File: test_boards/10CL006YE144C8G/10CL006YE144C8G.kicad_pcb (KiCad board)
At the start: 2 copper layers, 81 parts, among them IC401 10CL006YE144C8G, J401 CL_JTAG, U401 W25Q128JVS, Y401 SG-7050CAN

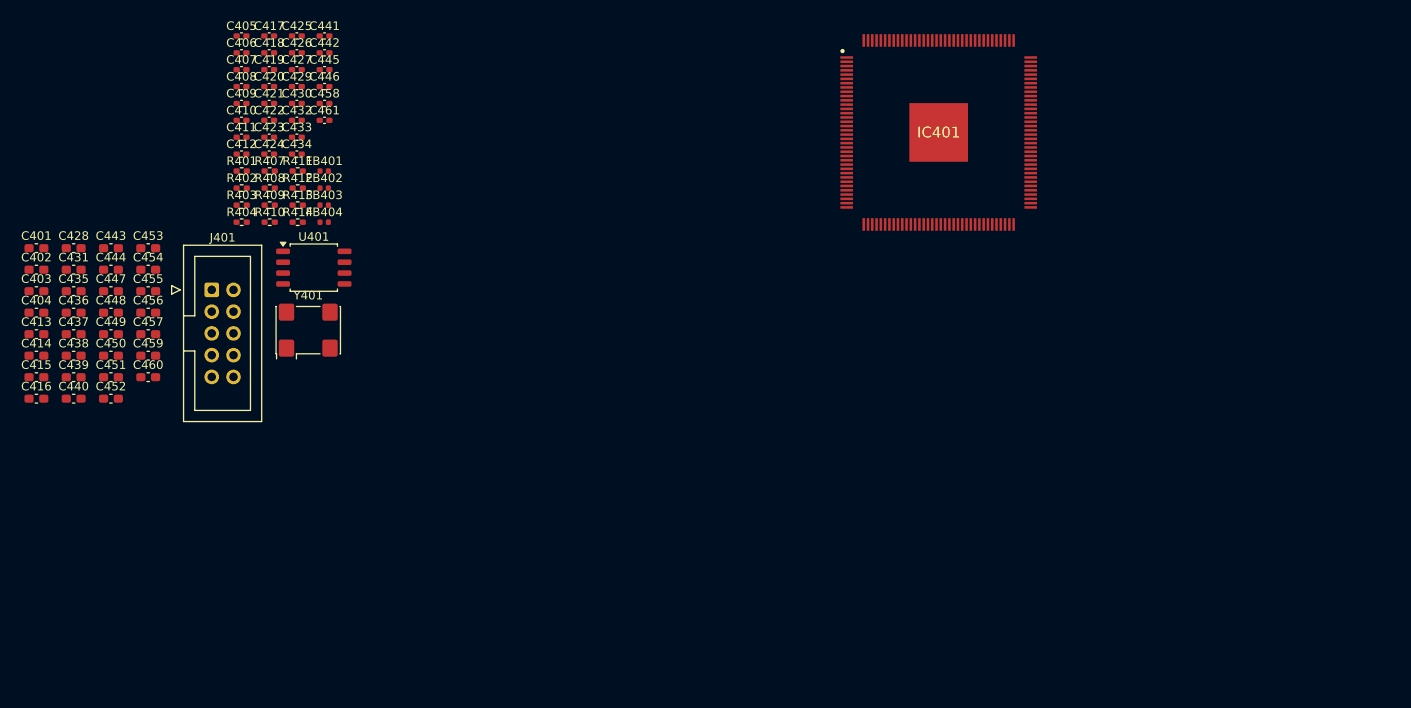
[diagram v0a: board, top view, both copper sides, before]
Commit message: Исправлена схема платы. Добавлен конфиг 10CL006.yaml
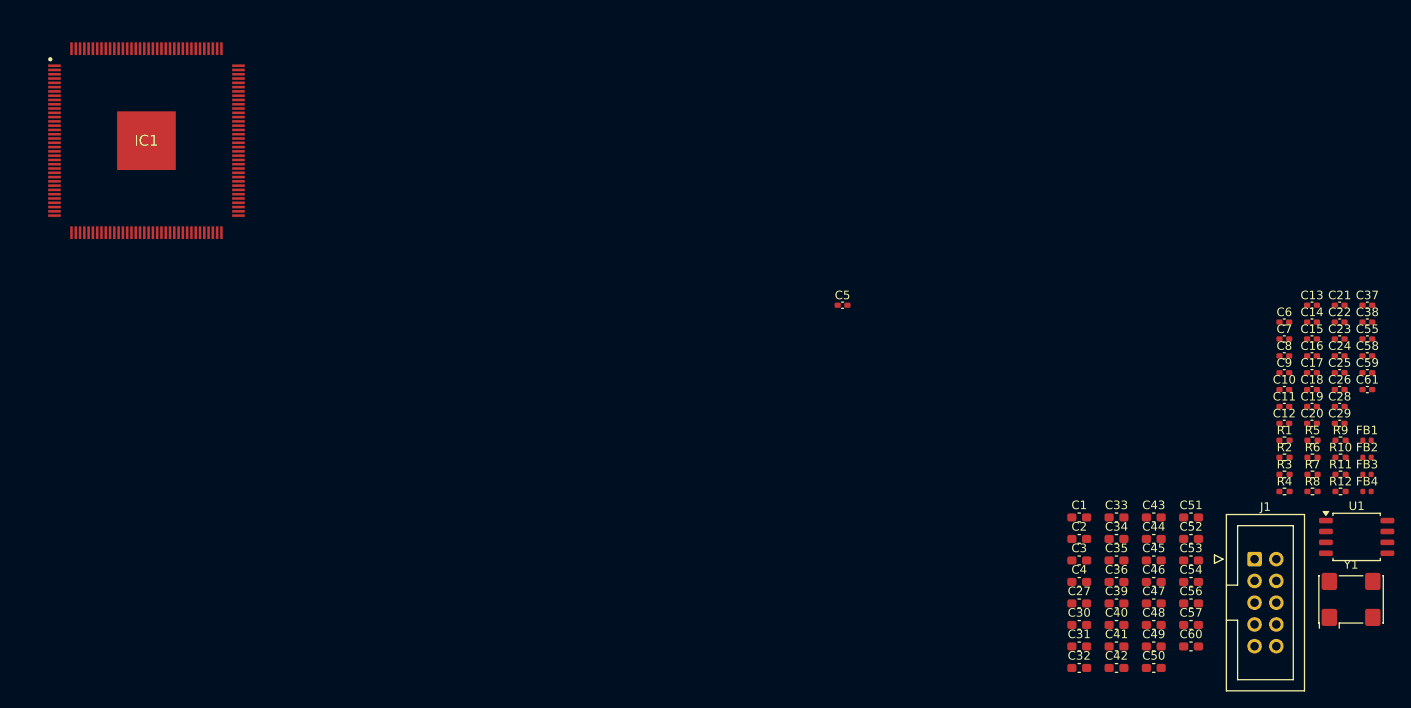
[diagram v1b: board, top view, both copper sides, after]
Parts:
- removed C401, C402, C403, C404, C435, C436, C437, C438, C439, C440, C443, C444: 1uF, Capacitor_SMD:C_0603_1608Metric_Pad1.08x0.95mm_HandSolder
- removed C405, C406, C407, C408, C409, C410, C411, C412, C417, C418, C419, C420, C421, C422, C423, C424, C425, C426, C427, C429, C430, C432, C433, C434, C441, C442, C445, C446, C458, C461: 100 nF, Capacitor_SMD:C_0402_1005Metric_Pad0.74x0.62mm_HandSolder
- removed C413, C414, C415, C416, C428, C431, C447, C448, C449, C450, C451, C452, C453, C454, C455, C456, C457, C459, C460: 4.7 uF, Capacitor_SMD:C_0603_1608Metric_Pad1.08x0.95mm_HandSolder
- removed FB401, FB402, FB403, FB404: BLM15PD121SN1D, Inductor_SMD:L_0402_1005Metric
- removed IC401: 10CL006YE144C8G, Custom_Altera_FPGA:QFP50P2200X2200X165-145N
- removed J401: CL_JTAG, Connector_IDC:IDC-Header_2x05_P2.54mm_Vertical
- removed R401: 33, Resistor_SMD:R_0402_1005Metric_Pad0.72x0.64mm_HandSolder
- removed R402, R403, R408, R409: 2R2, Resistor_SMD:R_0402_1005Metric_Pad0.72x0.64mm_HandSolder
- removed R404: 1K, Resistor_SMD:R_0402_1005Metric_Pad0.72x0.64mm_HandSolder
- removed R407, R413, R414: 4.7K, Resistor_SMD:R_0402_1005Metric_Pad0.72x0.64mm_HandSolder
- removed R410, R411, R412: 10K, Resistor_SMD:R_0402_1005Metric_Pad0.72x0.64mm_HandSolder
- removed U401: W25Q128JVS, Package_SO:SOIC-8_5.3x5.3mm_P1.27mm
- removed Y401: SG-7050CAN, Oscillator:Oscillator_SMD_SeikoEpson_SG8002CA-4Pin_7.0x5.0mm
- added C1: 1uF, Capacitor_SMD:C_0603_1608Metric_Pad1.08x0.95mm_HandSolder, F.Cu at (181.3, 115.7)
- added C10: 100 nF, Capacitor_SMD:C_0402_1005Metric_Pad0.74x0.62mm_HandSolder, F.Cu at (205.2, 100.8)
- added C11: 100 nF, Capacitor_SMD:C_0402_1005Metric_Pad0.74x0.62mm_HandSolder, F.Cu at (205.2, 102.8)
- added C12: 100 nF, Capacitor_SMD:C_0402_1005Metric_Pad0.74x0.62mm_HandSolder, F.Cu at (205.2, 104.7)
- added C13: 100 nF, Capacitor_SMD:C_0402_1005Metric_Pad0.74x0.62mm_HandSolder, F.Cu at (208.4, 90.9)
- added C14: 100 nF, Capacitor_SMD:C_0402_1005Metric_Pad0.74x0.62mm_HandSolder, F.Cu at (208.4, 92.9)
- added C15: 100 nF, Capacitor_SMD:C_0402_1005Metric_Pad0.74x0.62mm_HandSolder, F.Cu at (208.4, 94.9)
- added C16: 100 nF, Capacitor_SMD:C_0402_1005Metric_Pad0.74x0.62mm_HandSolder, F.Cu at (208.4, 96.8)
- added C17: 100 nF, Capacitor_SMD:C_0402_1005Metric_Pad0.74x0.62mm_HandSolder, F.Cu at (208.4, 98.8)
- added C18: 100 nF, Capacitor_SMD:C_0402_1005Metric_Pad0.74x0.62mm_HandSolder, F.Cu at (208.4, 100.8)
- added C19: 100 nF, Capacitor_SMD:C_0402_1005Metric_Pad0.74x0.62mm_HandSolder, F.Cu at (208.4, 102.8)
- added C2: 1uF, Capacitor_SMD:C_0603_1608Metric_Pad1.08x0.95mm_HandSolder, F.Cu at (181.3, 118.2)
- added C20: 100 nF, Capacitor_SMD:C_0402_1005Metric_Pad0.74x0.62mm_HandSolder, F.Cu at (208.4, 104.7)
- added C21: 100 nF, Capacitor_SMD:C_0402_1005Metric_Pad0.74x0.62mm_HandSolder, F.Cu at (211.7, 90.9)
- added C22: 100 nF, Capacitor_SMD:C_0402_1005Metric_Pad0.74x0.62mm_HandSolder, F.Cu at (211.7, 92.9)
- added C23: 100 nF, Capacitor_SMD:C_0402_1005Metric_Pad0.74x0.62mm_HandSolder, F.Cu at (211.7, 94.9)
- added C24: 100 nF, Capacitor_SMD:C_0402_1005Metric_Pad0.74x0.62mm_HandSolder, F.Cu at (211.7, 96.8)
- added C25: 100 nF, Capacitor_SMD:C_0402_1005Metric_Pad0.74x0.62mm_HandSolder, F.Cu at (211.7, 98.8)
- added C26: 100 nF, Capacitor_SMD:C_0402_1005Metric_Pad0.74x0.62mm_HandSolder, F.Cu at (211.7, 100.8)
- added C27: 4.7 uF, Capacitor_SMD:C_0603_1608Metric_Pad1.08x0.95mm_HandSolder, F.Cu at (181.3, 125.7)
- added C28: 100 nF, Capacitor_SMD:C_0402_1005Metric_Pad0.74x0.62mm_HandSolder, F.Cu at (211.7, 102.8)
- added C29: 100 nF, Capacitor_SMD:C_0402_1005Metric_Pad0.74x0.62mm_HandSolder, F.Cu at (211.7, 104.7)
- added C3: 1uF, Capacitor_SMD:C_0603_1608Metric_Pad1.08x0.95mm_HandSolder, F.Cu at (181.3, 120.7)
- added C30: 4.7 uF, Capacitor_SMD:C_0603_1608Metric_Pad1.08x0.95mm_HandSolder, F.Cu at (181.3, 128.3)
- added C31: 4.7 uF, Capacitor_SMD:C_0603_1608Metric_Pad1.08x0.95mm_HandSolder, F.Cu at (181.3, 130.8)
- added C32: 4.7 uF, Capacitor_SMD:C_0603_1608Metric_Pad1.08x0.95mm_HandSolder, F.Cu at (181.3, 133.3)
- added C33: 4.7 uF, Capacitor_SMD:C_0603_1608Metric_Pad1.08x0.95mm_HandSolder, F.Cu at (185.6, 115.7)
- added C34: 4.7 uF, Capacitor_SMD:C_0603_1608Metric_Pad1.08x0.95mm_HandSolder, F.Cu at (185.6, 118.2)
- added C35: 4.7 uF, Capacitor_SMD:C_0603_1608Metric_Pad1.08x0.95mm_HandSolder, F.Cu at (185.6, 120.7)
- added C36: 4.7 uF, Capacitor_SMD:C_0603_1608Metric_Pad1.08x0.95mm_HandSolder, F.Cu at (185.6, 123.2)
- added C37: 100 nF, Capacitor_SMD:C_0402_1005Metric_Pad0.74x0.62mm_HandSolder, F.Cu at (214.9, 90.9)
- added C38: 100 nF, Capacitor_SMD:C_0402_1005Metric_Pad0.74x0.62mm_HandSolder, F.Cu at (214.9, 92.9)
- added C39: 4.7 uF, Capacitor_SMD:C_0603_1608Metric_Pad1.08x0.95mm_HandSolder, F.Cu at (185.6, 125.7)
- added C4: 1uF, Capacitor_SMD:C_0603_1608Metric_Pad1.08x0.95mm_HandSolder, F.Cu at (181.3, 123.2)
- added C40: 4.7 uF, Capacitor_SMD:C_0603_1608Metric_Pad1.08x0.95mm_HandSolder, F.Cu at (185.6, 128.3)
- added C41: 4.7 uF, Capacitor_SMD:C_0603_1608Metric_Pad1.08x0.95mm_HandSolder, F.Cu at (185.6, 130.8)
- added C42: 4.7 uF, Capacitor_SMD:C_0603_1608Metric_Pad1.08x0.95mm_HandSolder, F.Cu at (185.6, 133.3)
- added C43: 4.7 uF, Capacitor_SMD:C_0603_1608Metric_Pad1.08x0.95mm_HandSolder, F.Cu at (190.0, 115.7)
- added C44: 4.7 uF, Capacitor_SMD:C_0603_1608Metric_Pad1.08x0.95mm_HandSolder, F.Cu at (190.0, 118.2)
- added C45: 4.7 uF, Capacitor_SMD:C_0603_1608Metric_Pad1.08x0.95mm_HandSolder, F.Cu at (190.0, 120.7)
- added C46: 1uF, Capacitor_SMD:C_0603_1608Metric_Pad1.08x0.95mm_HandSolder, F.Cu at (190.0, 123.2)
- added C47: 1uF, Capacitor_SMD:C_0603_1608Metric_Pad1.08x0.95mm_HandSolder, F.Cu at (190.0, 125.7)
- added C48: 1uF, Capacitor_SMD:C_0603_1608Metric_Pad1.08x0.95mm_HandSolder, F.Cu at (190.0, 128.3)
- added C49: 1uF, Capacitor_SMD:C_0603_1608Metric_Pad1.08x0.95mm_HandSolder, F.Cu at (190.0, 130.8)
- added C5: 100 nF, Capacitor_SMD:C_0402_1005Metric_Pad0.74x0.62mm_HandSolder, F.Cu at (153.6, 90.9)
- added C50: 4.7 uF, Capacitor_SMD:C_0603_1608Metric_Pad1.08x0.95mm_HandSolder, F.Cu at (190.0, 133.3)
- added C51: 4.7 uF, Capacitor_SMD:C_0603_1608Metric_Pad1.08x0.95mm_HandSolder, F.Cu at (194.3, 115.7)
- added C52: 4.7 uF, Capacitor_SMD:C_0603_1608Metric_Pad1.08x0.95mm_HandSolder, F.Cu at (194.3, 118.2)
- added C53: 4.7 uF, Capacitor_SMD:C_0603_1608Metric_Pad1.08x0.95mm_HandSolder, F.Cu at (194.3, 120.7)
- added C54: 1uF, Capacitor_SMD:C_0603_1608Metric_Pad1.08x0.95mm_HandSolder, F.Cu at (194.3, 123.2)
- added C55: 100 nF, Capacitor_SMD:C_0402_1005Metric_Pad0.74x0.62mm_HandSolder, F.Cu at (214.9, 94.9)
- added C56: 1uF, Capacitor_SMD:C_0603_1608Metric_Pad1.08x0.95mm_HandSolder, F.Cu at (194.3, 125.7)
- added C57: 1uF, Capacitor_SMD:C_0603_1608Metric_Pad1.08x0.95mm_HandSolder, F.Cu at (194.3, 128.3)
- added C58: 100 nF, Capacitor_SMD:C_0402_1005Metric_Pad0.74x0.62mm_HandSolder, F.Cu at (214.9, 96.8)
- added C59: 100 nF, Capacitor_SMD:C_0402_1005Metric_Pad0.74x0.62mm_HandSolder, F.Cu at (214.9, 98.8)
- added C6: 100 nF, Capacitor_SMD:C_0402_1005Metric_Pad0.74x0.62mm_HandSolder, F.Cu at (205.2, 92.9)
- added C60: 1uF, Capacitor_SMD:C_0603_1608Metric_Pad1.08x0.95mm_HandSolder, F.Cu at (194.3, 130.8)
- added C61: 100 nF, Capacitor_SMD:C_0402_1005Metric_Pad0.74x0.62mm_HandSolder, F.Cu at (214.9, 100.8)
- added C7: 100 nF, Capacitor_SMD:C_0402_1005Metric_Pad0.74x0.62mm_HandSolder, F.Cu at (205.2, 94.9)
- added C8: 100 nF, Capacitor_SMD:C_0402_1005Metric_Pad0.74x0.62mm_HandSolder, F.Cu at (205.2, 96.8)
- added C9: 100 nF, Capacitor_SMD:C_0402_1005Metric_Pad0.74x0.62mm_HandSolder, F.Cu at (205.2, 98.8)
- added FB1: BLM15PD121SN1D, Inductor_SMD:L_0402_1005Metric, F.Cu at (214.9, 106.7)
- added FB2: BLM15PD121SN1D, Inductor_SMD:L_0402_1005Metric, F.Cu at (214.9, 108.7)
- added FB3: BLM15PD121SN1D, Inductor_SMD:L_0402_1005Metric, F.Cu at (214.9, 110.7)
- added FB4: BLM15PD121SN1D, Inductor_SMD:L_0402_1005Metric, F.Cu at (214.9, 112.7)
- added IC1: 10CL006YE144C8G, Custom_Altera_FPGA:QFP50P2200X2200X165-145N, F.Cu at (72.4, 71.7)
- added J1: CL_JTAG, Connector_IDC:IDC-Header_2x05_P2.54mm_Vertical, F.Cu at (201.7, 120.6)
- added R1: 1K, Resistor_SMD:R_0402_1005Metric_Pad0.72x0.64mm_HandSolder, F.Cu at (205.2, 106.7)
- added R10: 10K, Resistor_SMD:R_0402_1005Metric_Pad0.72x0.64mm_HandSolder, F.Cu at (211.8, 108.7)
- added R11: 4.7K, Resistor_SMD:R_0402_1005Metric_Pad0.72x0.64mm_HandSolder, F.Cu at (211.8, 110.7)
- added R12: 4.7K, Resistor_SMD:R_0402_1005Metric_Pad0.72x0.64mm_HandSolder, F.Cu at (211.8, 112.7)
- added R2: 4.7K, Resistor_SMD:R_0402_1005Metric_Pad0.72x0.64mm_HandSolder, F.Cu at (205.2, 108.7)
- added R3: 33, Resistor_SMD:R_0402_1005Metric_Pad0.72x0.64mm_HandSolder, F.Cu at (205.2, 110.7)
- added R4: 2R2, Resistor_SMD:R_0402_1005Metric_Pad0.72x0.64mm_HandSolder, F.Cu at (205.2, 112.7)
- added R5: 2R2, Resistor_SMD:R_0402_1005Metric_Pad0.72x0.64mm_HandSolder, F.Cu at (208.5, 106.7)
- added R6: 2R2, Resistor_SMD:R_0402_1005Metric_Pad0.72x0.64mm_HandSolder, F.Cu at (208.5, 108.7)
- added R7: 2R2, Resistor_SMD:R_0402_1005Metric_Pad0.72x0.64mm_HandSolder, F.Cu at (208.5, 110.7)
- added R8: 10K, Resistor_SMD:R_0402_1005Metric_Pad0.72x0.64mm_HandSolder, F.Cu at (208.5, 112.7)
- added R9: 10K, Resistor_SMD:R_0402_1005Metric_Pad0.72x0.64mm_HandSolder, F.Cu at (211.8, 106.7)
- added U1: W25Q128JVS, Package_SO:SOIC-8_5.3x5.3mm_P1.27mm, F.Cu at (213.6, 118.0)
- added Y1: SG-7050CAN, Oscillator:Oscillator_SMD_SeikoEpson_SG8002CA-4Pin_7.0x5.0mm, F.Cu at (213.0, 125.3)
